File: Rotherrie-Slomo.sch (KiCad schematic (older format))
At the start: 5 parts, among them J1 CONN_02X08

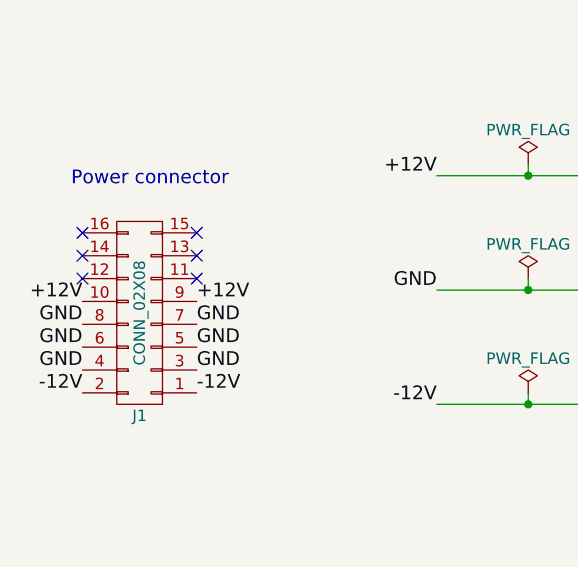
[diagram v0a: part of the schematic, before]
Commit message: Part associations made. 16pin connector reduced to 10 pin
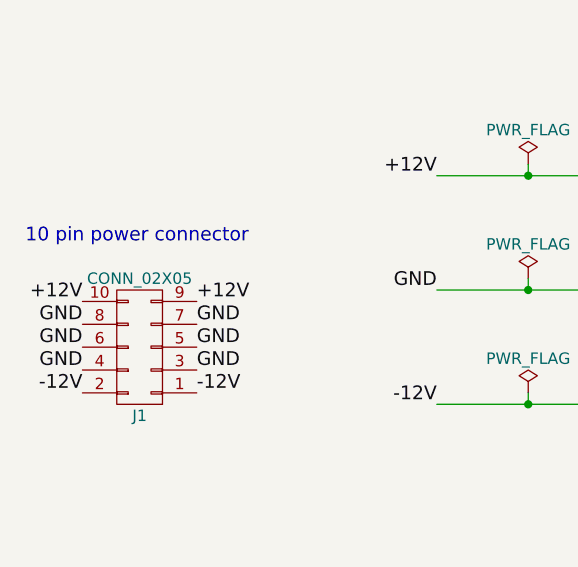
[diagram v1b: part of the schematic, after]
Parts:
- removed J1: CONN_02X08, symbol CONN_02X08
- added J1: CONN_02X05, symbol CONN_02X05
- C1, C2: footprint (none) -> Capacitors_THT:CP_Radial_D7.5mm_P2.50mm
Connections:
- net GND: now also J1.3 (P3), J1.4 (P4), J1.5 (P5), J1.6 (P6), J1.7 (P7), J1.8 (P8)
- net VCC: now also J1.10 (P10), J1.9 (P9)
- net VEE: now also J1.1 (P1), J1.2 (P2)
- no-connect marks 6 -> 0
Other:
- note added: "10 pin power connector"
- note removed: "Power connector"
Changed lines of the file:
@@
 Comment4 ""
 $EndDescr
-$Comp
-L CONN_02X08 J1
-U 1 1 59B14829
-P 1800 2600
-F 0 "J1" H 1800 3050 50  0000 C CNN
-F 1 "CONN_02X08" V 1800 2600 50  0000 C CNN
-F 2 "" H 1800 1400 50  0001 C CNN
-F 3 "" H 1800 1400 50  0001 C CNN
-	1    1800 2600
-	-1   0    0    1
-$EndComp
-Text Notes 1500 2050 0    60   ~ 0
-Power connector
-NoConn ~ 1550 2250
-NoConn ~ 1550 2350
-NoConn ~ 1550 2450
-NoConn ~ 2050 2450
-NoConn ~ 2050 2350
-NoConn ~ 2050 2250
+Text Notes 1300 2300 0    60   ~ 0
+10 pin power connector
 Text Label 2050 2550 0    60   ~ 0
 +12V
@@
 F 0 "C1" H 4825 2350 50  0000 L CNN
 F 1 "22uF" H 4825 2150 50  0000 L CNN
-F 2 "" H 4838 2100 50  0001 C CNN
+F 2 "Capacitors_THT:CP_Radial_D7.5mm_P2.50mm" H 4838 2100 50  0001 C CNN
 F 3 "" H 4800 2250 50  0001 C CNN
 	1    4800 2250
@@
 F 0 "C2" H 4825 2850 50  0000 L CNN
 F 1 "22uF" H 4825 2650 50  0000 L CNN
-F 2 "" H 4838 2600 50  0001 C CNN
+F 2 "Capacitors_THT:CP_Radial_D7.5mm_P2.50mm" H 4838 2600 50  0001 C CNN
 F 3 "" H 4800 2750 50  0001 C CNN
 	1    4800 2750
@@
 F1 "Rotherrie-Slomo-002.sch" 60
 $EndSheet
+$Comp
+L CONN_02X05 J1
+U 1 1 59B28D47
+P 1800 2750
+F 0 "J1" H 1800 3050 50  0000 C CNN
+F 1 "CONN_02X05" H 1800 2450 50  0000 C CNN
+F 2 "" H 1800 1550 50  0001 C CNN
+F 3 "" H 1800 1550 50  0001 C CNN
+	1    1800 2750
+	-1   0    0    1
+$EndComp
 $EndSCHEMATC

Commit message: Added jack connectors to schematic
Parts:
- D1, D2: footprint (none) -> Diodes_THT:D_DO-41_SOD81_P7.62mm_Horizontal
- J1: footprint (none) -> Pin_Headers:Pin_Header_Straight_2x05_Pitch2.54mm
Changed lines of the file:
@@
 F 0 "D1" H 4000 2350 50  0000 C CNN
 F 1 "1N5817" H 4000 2150 50  0000 C CNN
-F 2 "" H 4000 2250 50  0001 C CNN
+F 2 "Diodes_THT:D_DO-41_SOD81_P7.62mm_Horizontal" H 4000 2250 50  0001 C CNN
 F 3 "" H 4000 2250 50  0001 C CNN
 	1    4000 2250
@@
 F 0 "D2" H 4000 2850 50  0000 C CNN
 F 1 "1N5817" H 4000 2650 50  0000 C CNN
-F 2 "" H 4000 2750 50  0001 C CNN
+F 2 "Diodes_THT:D_DO-41_SOD81_P7.62mm_Horizontal" H 4000 2750 50  0001 C CNN
 F 3 "" H 4000 2750 50  0001 C CNN
 	1    4000 2750
@@
 F 0 "J1" H 1800 3050 50  0000 C CNN
 F 1 "CONN_02X05" H 1800 2450 50  0000 C CNN
-F 2 "" H 1800 1550 50  0001 C CNN
+F 2 "Pin_Headers:Pin_Header_Straight_2x05_Pitch2.54mm" H 1800 1550 50  0001 C CNN
 F 3 "" H 1800 1550 50  0001 C CNN
 	1    1800 2750

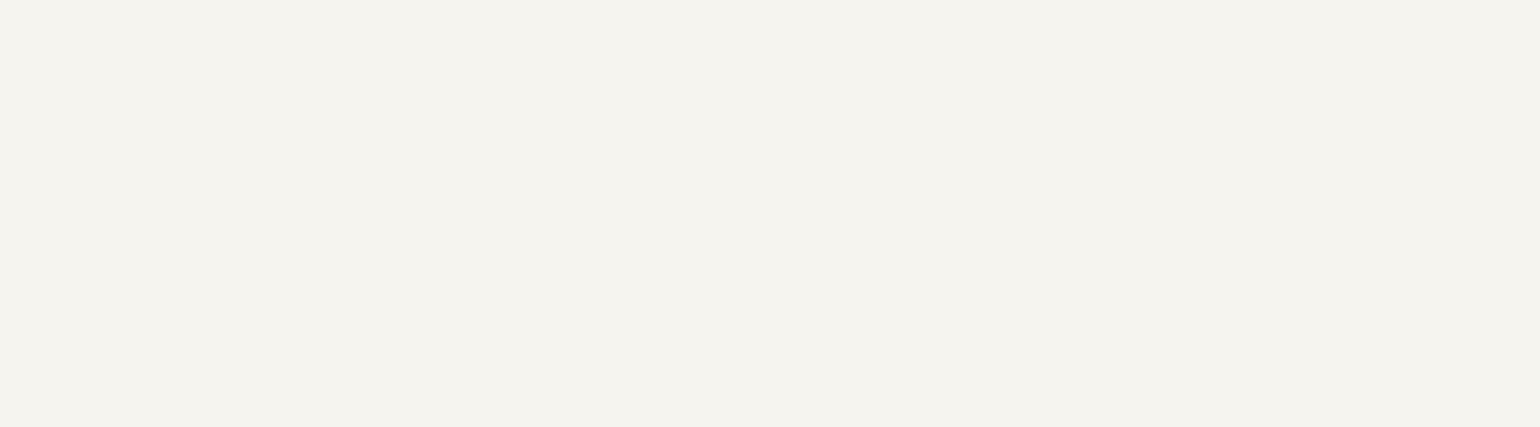
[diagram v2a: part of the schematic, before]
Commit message: Rerouting from logic to controller board
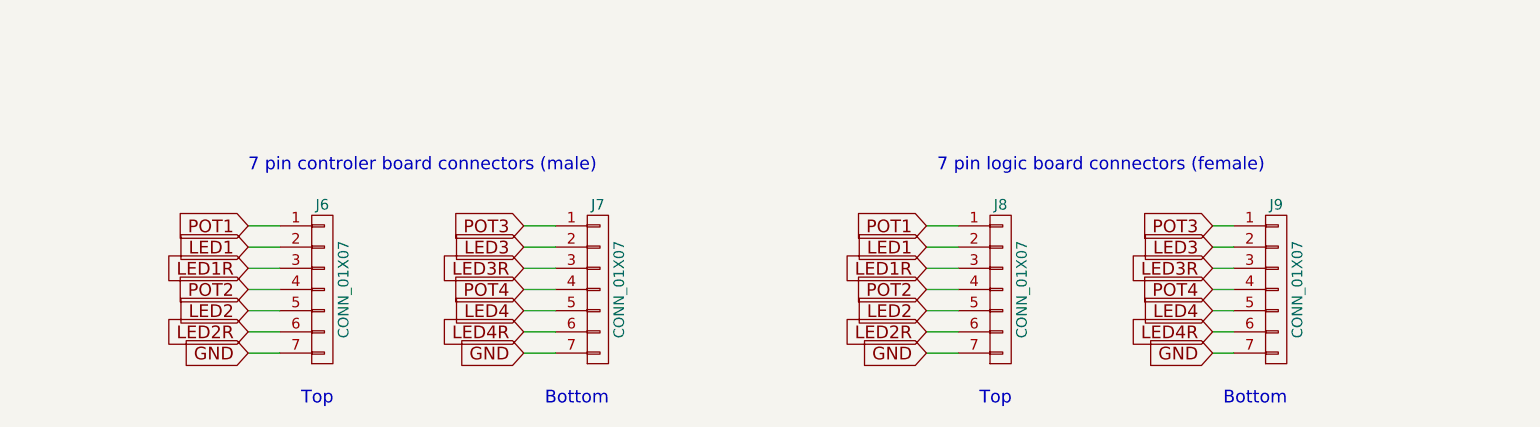
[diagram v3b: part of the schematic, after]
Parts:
- added J6, J7, J8, J9: CONN_01X07, Pin_Headers:Pin_Header_Straight_1x07_Pitch2.54mm, symbol CONN_01X07
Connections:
- net GND: now also J6.7 (P7), J7.7 (P7), J8.7 (P7), J9.7 (P7)
- new net LED1: J6.2 (P2), J8.2 (P2)
- new net LED1R: J6.3 (P3), J8.3 (P3)
- new net LED2: J6.5 (P5), J8.5 (P5)
- new net LED2R: J6.6 (P6), J8.6 (P6)
- new net LED3: J7.2 (P2), J9.2 (P2)
- new net LED3R: J7.3 (P3), J9.3 (P3)
- new net LED4: J7.5 (P5), J9.5 (P5)
- new net LED4R: J7.6 (P6), J9.6 (P6)
- new net POT1: J6.1 (P1), J8.1 (P1)
- new net POT2: J6.4 (P4), J8.4 (P4)
- new net POT3: J7.1 (P1), J9.1 (P1)
- new net POT4: J7.4 (P4), J9.4 (P4)
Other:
- note added: "7 pin controler board connectors (male)"
- note added: "7 pin logic board connectors (female)"
- note added: "Bottom"
- note added: "Top"
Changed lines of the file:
@@
 	-1   0    0    1
 $EndComp
+$Comp
+L CONN_01X07 J6
+U 1 1 59B2A9BA
+P 4100 4750
+F 0 "J6" H 4100 5150 50  0000 C CNN
+F 1 "CONN_01X07" V 4200 4750 50  0000 C CNN
+F 2 "Pin_Headers:Pin_Header_Straight_1x07_Pitch2.54mm" H 4100 4750 50  0001 C CNN
+F 3 "" H 4100 4750 50  0001 C CNN
+	1    4100 4750
+	1    0    0    -1
+$EndComp
+$Comp
+L CONN_01X07 J7
+U 1 1 59B2A9EF
+P 5400 4750
+F 0 "J7" H 5400 5150 50  0000 C CNN
+F 1 "CONN_01X07" V 5500 4750 50  0000 C CNN
+F 2 "Pin_Headers:Pin_Header_Straight_1x07_Pitch2.54mm" H 5400 4750 50  0001 C CNN
+F 3 "" H 5400 4750 50  0001 C CNN
+	1    5400 4750
+	1    0    0    -1
+$EndComp
+Text Notes 3750 4200 0    60   ~ 0
+7 pin controler board connectors (male)
+Text Notes 4000 5300 0    60   ~ 0
+Top
+Text Notes 5150 5300 0    60   ~ 0
+Bottom
+$Comp
+L CONN_01X07 J8
+U 1 1 59B2ABA1
+P 7300 4750
+F 0 "J8" H 7300 5150 50  0000 C CNN
+F 1 "CONN_01X07" V 7400 4750 50  0000 C CNN
+F 2 "Pin_Headers:Pin_Header_Straight_1x07_Pitch2.54mm" H 7300 4750 50  0001 C CNN
+F 3 "" H 7300 4750 50  0001 C CNN
+	1    7300 4750
+	1    0    0    -1
+$EndComp
+$Comp
+L CONN_01X07 J9
+U 1 1 59B2ABA7
+P 8600 4750
+F 0 "J9" H 8600 5150 50  0000 C CNN
+F 1 "CONN_01X07" V 8700 4750 50  0000 C CNN
+F 2 "Pin_Headers:Pin_Header_Straight_1x07_Pitch2.54mm" H 8600 4750 50  0001 C CNN
+F 3 "" H 8600 4750 50  0001 C CNN
+	1    8600 4750
+	1    0    0    -1
+$EndComp
+Text Notes 7000 4200 0    60   ~ 0
+7 pin logic board connectors (female)
+Text Notes 7200 5300 0    60   ~ 0
+Top
+Text Notes 8350 5300 0    60   ~ 0
+Bottom
+Text GLabel 3750 4450 0    60   Input ~ 0
+POT1
+Text GLabel 3750 4550 0    60   Input ~ 0
+LED1
+Text GLabel 3750 4650 0    60   Input ~ 0
+LED1R
+Text GLabel 3750 4750 0    60   Input ~ 0
+POT2
+Text GLabel 3750 4850 0    60   Input ~ 0
+LED2
+Text GLabel 3750 4950 0    60   Input ~ 0
+LED2R
+Text GLabel 3750 5050 0    60   Input ~ 0
+GND
+Text GLabel 5050 4450 0    60   Input ~ 0
+POT3
+Text GLabel 5050 4550 0    60   Input ~ 0
+LED3
+Text GLabel 5050 5050 0    60   Input ~ 0
+GND
+Wire Wire Line
+	3750 4450 3900 4450
+Wire Wire Line
+	3750 4550 3900 4550
+Wire Wire Line
+	3750 4650 3900 4650
+Wire Wire Line
+	3750 4750 3900 4750
+Wire Wire Line
+	3750 4850 3900 4850
+Wire Wire Line
+	3750 4950 3900 4950
+Wire Wire Line
+	3750 5050 3900 5050
+Wire Wire Line
+	5050 4450 5200 4450
+Wire Wire Line
+	5050 4550 5200 4550
+Wire Wire Line
+	5050 4650 5200 4650
+Wire Wire Line
+	5050 4750 5200 4750
+Wire Wire Line
+	5050 4850 5200 4850
+Wire Wire Line
+	5050 4950 5200 4950
+Wire Wire Line
+	5050 5050 5200 5050
+Wire Wire Line
+	6950 4450 7100 4450
+Wire Wire Line
+	6950 4550 7100 4550
+Wire Wire Line
+	6950 4650 7100 4650
+Wire Wire Line
+	6950 4750 7100 4750
+Wire Wire Line
+	6950 4850 7100 4850
+Wire Wire Line
+	6950 4950 7100 4950
+Wire Wire Line
+	6950 5050 7100 5050
+Wire Wire Line
+	8300 4450 8400 4450
+Wire Wire Line
+	8300 4550 8400 4550
+Wire Wire Line
+	8300 4650 8400 4650
+Wire Wire Line
+	8300 4750 8400 4750
+Wire Wire Line
+	8300 4850 8400 4850
+Wire Wire Line
+	8300 4950 8400 4950
+Wire Wire Line
+	8300 5050 8400 5050
+Text GLabel 5050 4650 0    60   Input ~ 0
+LED3R
+Text GLabel 5050 4750 0    60   Input ~ 0
+POT4
+Text GLabel 5050 4850 0    60   Input ~ 0
+LED4
+Text GLabel 5050 4950 0    60   Input ~ 0
+LED4R
+Text GLabel 6950 4450 0    60   Input ~ 0
+POT1
+Text GLabel 6950 4550 0    60   Input ~ 0
+LED1
+Text GLabel 6950 4650 0    60   Input ~ 0
+LED1R
+Text GLabel 6950 4750 0    60   Input ~ 0
+POT2
+Text GLabel 6950 4850 0    60   Input ~ 0
+LED2
+Text GLabel 6950 4950 0    60   Input ~ 0
+LED2R
+Text GLabel 6950 5050 0    60   Input ~ 0
+GND
+Text GLabel 8300 4450 0    60   Input ~ 0
+POT3
+Text GLabel 8300 4550 0    60   Input ~ 0
+LED3
+Text GLabel 8300 5050 0    60   Input ~ 0
+GND
+Text GLabel 8300 4650 0    60   Input ~ 0
+LED3R
+Text GLabel 8300 4750 0    60   Input ~ 0
+POT4
+Text GLabel 8300 4850 0    60   Input ~ 0
+LED4
+Text GLabel 8300 4950 0    60   Input ~ 0
+LED4R
 $EndSCHEMATC

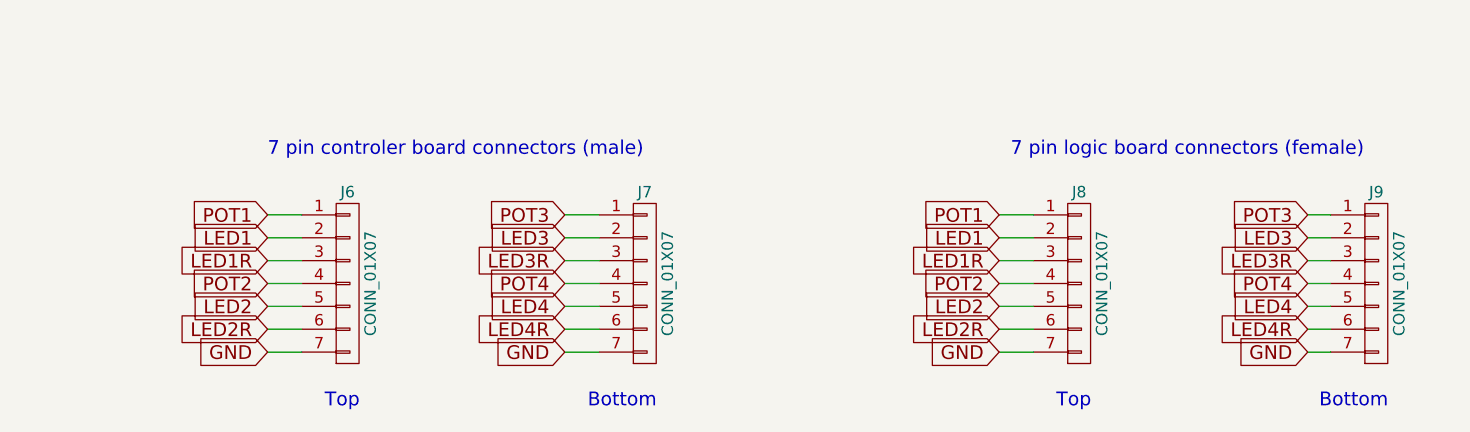
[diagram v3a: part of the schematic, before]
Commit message: Reroute controller board
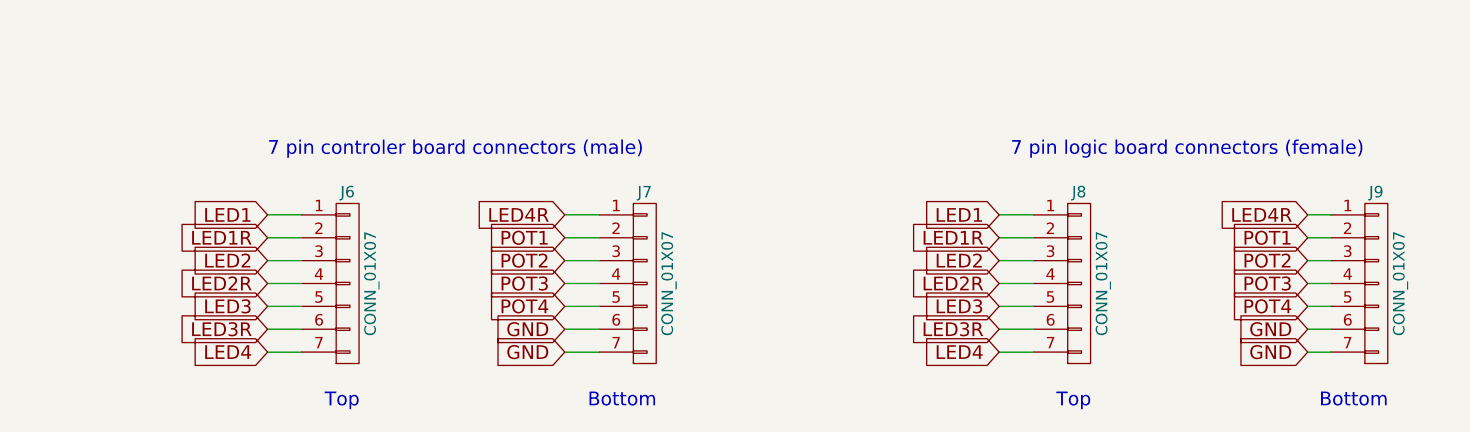
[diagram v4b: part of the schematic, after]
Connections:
- net GND: now also J7.6 (P6), J9.6 (P6); no longer J6.7 (P7), J8.7 (P7)
- net LED1: now also J6.1 (P1), J8.1 (P1); no longer J6.2 (P2), J8.2 (P2)
- net LED1R: now also J6.2 (P2), J8.2 (P2); no longer J6.3 (P3), J8.3 (P3)
- net LED2: now also J6.3 (P3), J8.3 (P3); no longer J6.5 (P5), J8.5 (P5)
- net LED2R: now also J6.4 (P4), J8.4 (P4); no longer J6.6 (P6), J8.6 (P6)
- net LED3: now also J6.5 (P5), J8.5 (P5); no longer J7.2 (P2), J9.2 (P2)
- net LED3R: now also J6.6 (P6), J8.6 (P6); no longer J7.3 (P3), J9.3 (P3)
- net LED4: now also J6.7 (P7), J8.7 (P7); no longer J7.5 (P5), J9.5 (P5)
- net LED4R: now also J7.1 (P1), J9.1 (P1); no longer J7.6 (P6), J9.6 (P6)
- net POT1: now also J7.2 (P2), J9.2 (P2); no longer J6.1 (P1), J8.1 (P1)
- net POT2: now also J7.3 (P3), J9.3 (P3); no longer J6.4 (P4), J8.4 (P4)
- net POT3: now also J7.4 (P4), J9.4 (P4); no longer J7.1 (P1), J9.1 (P1)
- net POT4: now also J7.5 (P5), J9.5 (P5); no longer J7.4 (P4), J9.4 (P4)
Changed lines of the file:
@@
 Text Notes 8350 5300 0    60   ~ 0
 Bottom
+Text GLabel 5050 4550 0    60   Input ~ 0
+POT1
 Text GLabel 3750 4450 0    60   Input ~ 0
-POT1
+LED1
 Text GLabel 3750 4550 0    60   Input ~ 0
-LED1
+LED1R
+Text GLabel 5050 4650 0    60   Input ~ 0
+POT2
 Text GLabel 3750 4650 0    60   Input ~ 0
-LED1R
+LED2
 Text GLabel 3750 4750 0    60   Input ~ 0
-POT2
+LED2R
+Text GLabel 5050 4950 0    60   Input ~ 0
+GND
+Text GLabel 5050 4750 0    60   Input ~ 0
+POT3
 Text GLabel 3750 4850 0    60   Input ~ 0
-LED2
-Text GLabel 3750 4950 0    60   Input ~ 0
-LED2R
-Text GLabel 3750 5050 0    60   Input ~ 0
-GND
-Text GLabel 5050 4450 0    60   Input ~ 0
-POT3
-Text GLabel 5050 4550 0    60   Input ~ 0
 LED3
 Text GLabel 5050 5050 0    60   Input ~ 0
@@
 Wire Wire Line
 	8300 5050 8400 5050
-Text GLabel 5050 4650 0    60   Input ~ 0
+Text GLabel 3750 4950 0    60   Input ~ 0
 LED3R
-Text GLabel 5050 4750 0    60   Input ~ 0
+Text GLabel 5050 4850 0    60   Input ~ 0
 POT4
-Text GLabel 5050 4850 0    60   Input ~ 0
+Text GLabel 3750 5050 0    60   Input ~ 0
 LED4
-Text GLabel 5050 4950 0    60   Input ~ 0
+Text GLabel 5050 4450 0    60   Input ~ 0
 LED4R
 Text GLabel 6950 4450 0    60   Input ~ 0
+LED1
+Text GLabel 6950 4550 0    60   Input ~ 0
+LED1R
+Text GLabel 6950 4650 0    60   Input ~ 0
+LED2
+Text GLabel 6950 4750 0    60   Input ~ 0
+LED2R
+Text GLabel 6950 4850 0    60   Input ~ 0
+LED3
+Text GLabel 6950 4950 0    60   Input ~ 0
+LED3R
+Text GLabel 6950 5050 0    60   Input ~ 0
+LED4
+Text GLabel 8300 4550 0    60   Input ~ 0
 POT1
-Text GLabel 6950 4550 0    60   Input ~ 0
-LED1
-Text GLabel 6950 4650 0    60   Input ~ 0
-LED1R
-Text GLabel 6950 4750 0    60   Input ~ 0
+Text GLabel 8300 4650 0    60   Input ~ 0
 POT2
-Text GLabel 6950 4850 0    60   Input ~ 0
-LED2
-Text GLabel 6950 4950 0    60   Input ~ 0
-LED2R
-Text GLabel 6950 5050 0    60   Input ~ 0
+Text GLabel 8300 4950 0    60   Input ~ 0
 GND
-Text GLabel 8300 4450 0    60   Input ~ 0
+Text GLabel 8300 4750 0    60   Input ~ 0
 POT3
-Text GLabel 8300 4550 0    60   Input ~ 0
-LED3
 Text GLabel 8300 5050 0    60   Input ~ 0
 GND
-Text GLabel 8300 4650 0    60   Input ~ 0
-LED3R
-Text GLabel 8300 4750 0    60   Input ~ 0
+Text GLabel 8300 4850 0    60   Input ~ 0
 POT4
-Text GLabel 8300 4850 0    60   Input ~ 0
-LED4
-Text GLabel 8300 4950 0    60   Input ~ 0
+Text GLabel 8300 4450 0    60   Input ~ 0
 LED4R
 $EndSCHEMATC
